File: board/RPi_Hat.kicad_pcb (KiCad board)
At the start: 2 copper layers, 65 x 56.5 mm, 5 parts, among them J1 RPi_GPIO

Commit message: first draft of the HAT layout
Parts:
- added C1: 10µF, Capacitors_SMD:c_elec_4x4.5, F.Cu at (113.4, 56.0)
- added C2: 0.1µF, Capacitors_SMD:C_0805_HandSoldering, F.Cu at (108.9, 56.4)
- added C3: 1µF, Capacitors_SMD:C_1206_HandSoldering, F.Cu at (127.5, 78.5)
- added C4: 1µF, Capacitors_SMD:C_1206_HandSoldering, F.Cu at (127.5, 73.0)
- added C5: 0.1µF, Capacitors_SMD:C_0805_HandSoldering, F.Cu at (133.0, 68.0)
- added C6: 0.1µF, Capacitors_SMD:C_0805_HandSoldering, F.Cu at (104.5, 72.0)
- added C7: 22pF, Capacitors_SMD:C_0603_HandSoldering, F.Cu at (106.0, 57.0)
- added C8: 22pF, Capacitors_SMD:C_0603_HandSoldering, F.Cu at (85.7, 56.9)
- added D1: SMD_LED, LEDs:LED-1206, F.Cu at (116.0, 93.5)
- added I1: TC1108, TO_SOT_Packages_SMD:SOT-223, F.Cu at (117.0, 75.5)
- added IC1: ATMEGA328P-P, Housings_DIP:DIP-28_W7.62mm, F.Cu at (117.5, 61.0)
- added IC2: RFM69HW, mysensors-kicad:RFM69HW_SMD_Handsoldering, F.Cu at (86.5, 95.0)
- added JPR1: NC_JPR, Pin_Headers:Pin_Header_Straight_1x02, F.Cu at (116.0, 85.5)
- added P1: FTDI_CONN_01X06, Pin_Headers:Pin_Header_Straight_1x06, F.Cu at (138.0, 55.5)
- added P2: BATT_IN, Pin_Headers:Pin_Header_Angled_1x02, F.Cu at (135.0, 74.5)
- added P3: V_SRC_JPR, Pin_Headers:Pin_Header_Straight_1x03, F.Cu at (128.5, 67.5)
- added P4: UART_SRC_JPR, Pin_Headers:Pin_Header_Straight_2x03, F.Cu at (125.0, 67.5)
- added P5: LED_CONN, Pin_Headers:Pin_Header_Straight_1x02, F.Cu at (116.0, 99.0)
- added P6: SW_CONN, Pin_Headers:Pin_Header_Straight_1x02, F.Cu at (130.5, 99.0)
- added P7: CONN_01X01, Pin_Headers:Pin_Header_Straight_1x01, F.Cu at (98.5, 74.0)
- added Q1: BSS138_GSD, TO_SOT_Packages_SMD:SOT-23_Handsoldering, F.Cu at (129.1, 55.7)
- added R1: 10K, Resistors_SMD:R_0805_HandSoldering, F.Cu at (124.9, 55.5)
- added R2: 10K, Resistors_SMD:R_0805_HandSoldering, F.Cu at (134.0, 55.6)
- added R3: 560R, Resistors_SMD:R_0603_HandSoldering, F.Cu at (116.0, 90.0)
- added R4: 10K, Resistors_SMD:R_0805_HandSoldering, F.Cu at (138.5, 87.5)
- added R5: 10K, Resistors_SMD:R_0805_HandSoldering, F.Cu at (133.0, 62.5)
- added SW1: SWITCH, Buttons_Switches_ThroughHole:SW_PUSH, F.Cu at (129.5, 88.0)
- added Y1: 16MHz, Crystals_Oscillators_SMD:Q_49U3HMS, F.Cu at (96.0, 56.0)
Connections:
- J1 pad 1: Net-(J1-Pad1) -> V3.3_PI
- J1 pad 10: Net-(J1-Pad10) -> RX_PI
- J1 pad 14: Net-(J1-Pad14) -> GND
- J1 pad 17: Net-(J1-Pad17) -> V3.3_PI
- J1 pad 20: Net-(J1-Pad20) -> GND
- J1 pad 25: Net-(J1-Pad25) -> GND
- J1 pad 30: Net-(J1-Pad30) -> GND
- J1 pad 34: Net-(J1-Pad34) -> GND
- J1 pad 39: Net-(J1-Pad39) -> GND
- J1 pad 6: Net-(J1-Pad6) -> GND
- J1 pad 8: Net-(J1-Pad8) -> TX_PI
- J1 pad 9: Net-(J1-Pad9) -> GND
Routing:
- net V3.3: track 0.00 -> 150.9 mm, vias 0 -> 2
- net SW_D3: track 0.00 -> 68.2 mm
- net LED_D9: track 0.00 -> 63.3 mm
- net V3.3_PI: track 0.00 -> 54.3 mm, vias 0 -> 2
- net D2_INT0: track 0.00 -> 50.4 mm, vias 0 -> 1
- net RX_PI: track 0.00 -> 47.1 mm, vias 0 -> 2
- net TX_PI: track 0.00 -> 46.4 mm, vias 0 -> 2
- net +BATT: track 0.00 -> 45.7 mm, vias 0 -> 1
- net TX_FTDI: track 0.00 -> 29.4 mm, vias 0 -> 2
- net Net-(C5-Pad2): track 0.00 -> 24.8 mm, vias 0 -> 1
- net RX_FTDI: track 0.00 -> 17.0 mm
- net TX_IN: track 0.00 -> 16.6 mm
- net TX_ARD: track 0.00 -> 15.2 mm
- net Net-(C8-Pad2): track 0.00 -> 13.0 mm
- net Net-(C7-Pad2): track 0.00 -> 12.8 mm
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
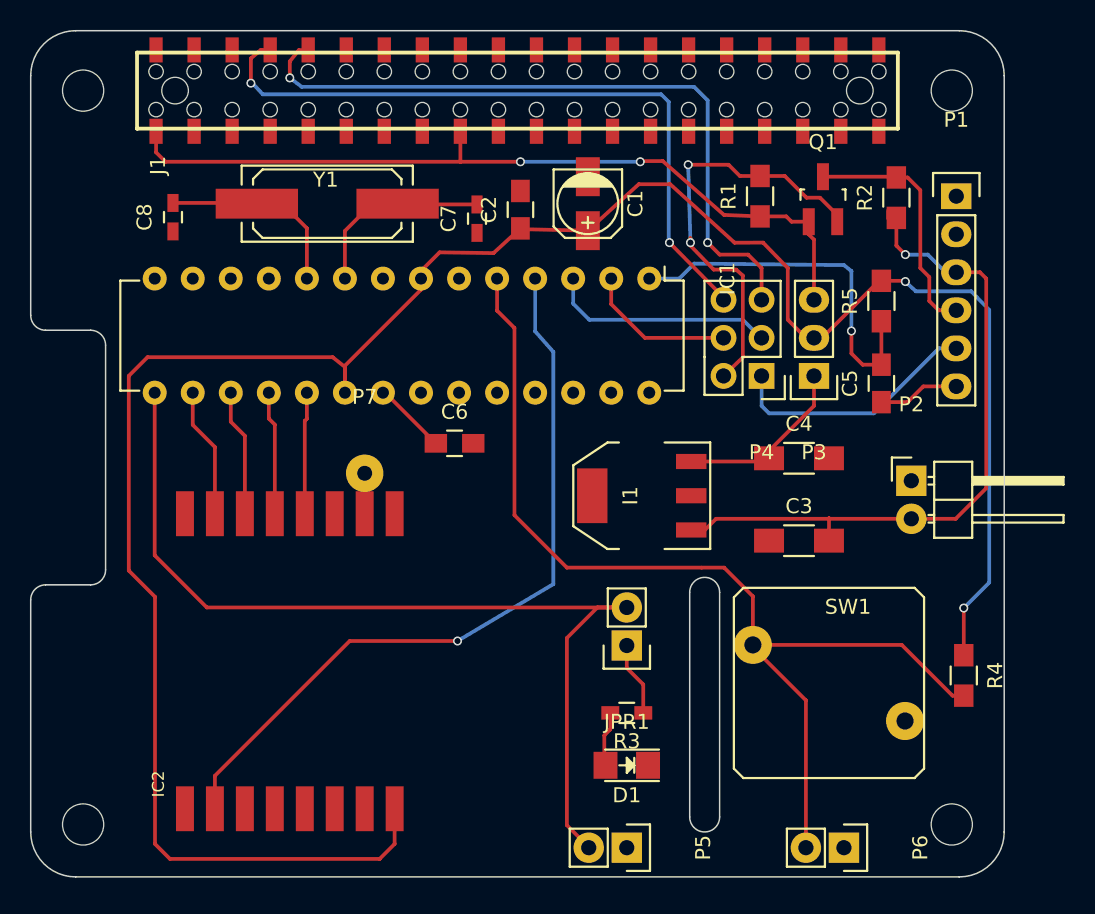
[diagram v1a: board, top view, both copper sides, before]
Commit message: board layout. check before manufacture
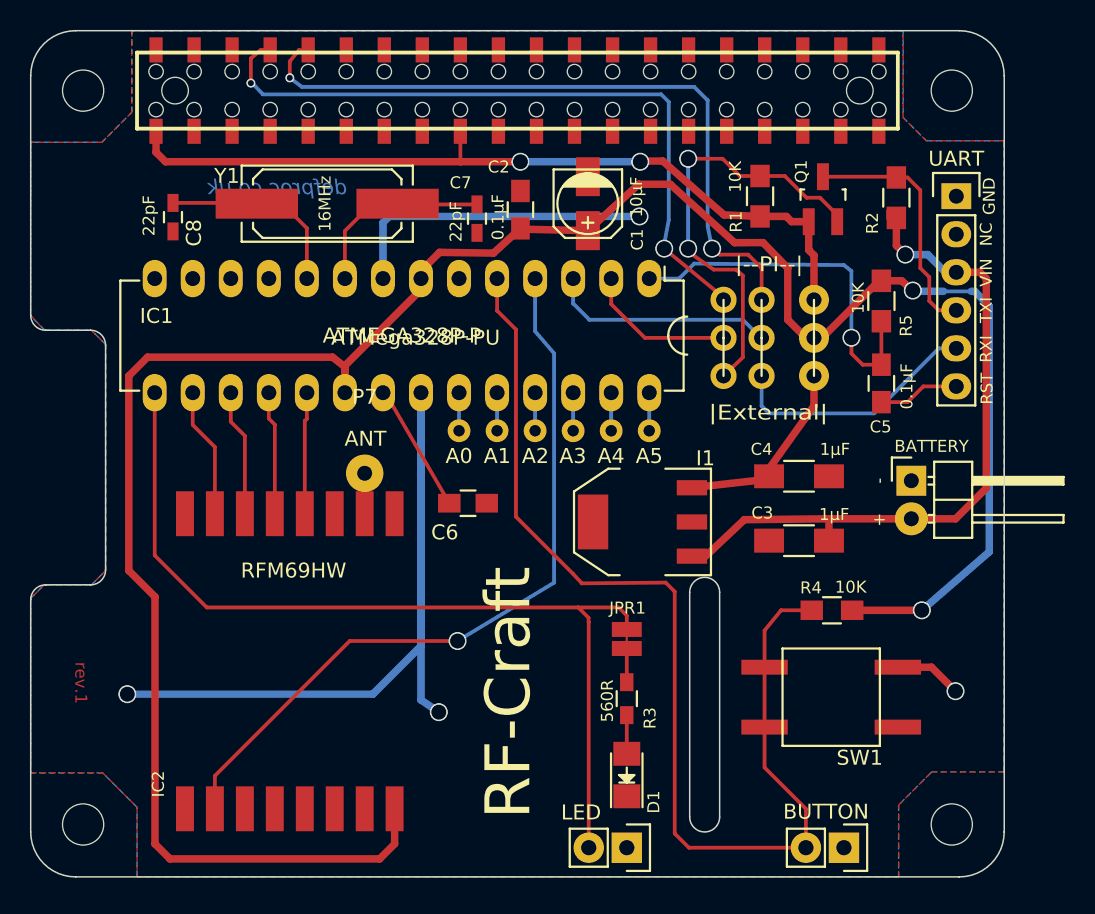
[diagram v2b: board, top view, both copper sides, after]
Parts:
- BATTERY: renamed from P2; footprint Pin_Headers:Pin_Header_Angled_1x02 -> Pin_Header_Angled_1x02
- BUTTON: renamed from P3; footprint Pin_Headers:Pin_Header_Straight_1x03 -> Pin_Header_Straight_1x03
- IC1: footprint Housings_DIP:DIP-28_W7.62mm -> A0-A5_DIP-28_W7.62mm
- JPR1: footprint Pin_Headers:Pin_Header_Straight_1x02 -> NC_SMD_JPR
- P: renamed from P4; footprint Pin_Headers:Pin_Header_Straight_2x03 -> Pin_Header_Straight_2x03
- SW1: footprint Buttons_Switches_ThroughHole:SW_PUSH -> KSEx00G_SW
- UART: renamed from P1; footprint Pin_Headers:Pin_Header_Straight_1x06 -> Pin_Header_Straight_1x06
- moved R4 9.82 mm to (129.7, 83.2), turned to 180 degrees
- moved C6 4.10 mm to (105.4, 76.0)
- moved I1 1.75 mm to (117.0, 77.2)
- moved C4 1.20 mm to (127.5, 74.2)
- moved SW1 0.96 mm to (129.7, 89.0)
- moved R3 0.95 mm to (116.0, 89.0), turned to 270 degrees
- moved D1 0.65 mm to (116.0, 94.2), turned to 90 degrees
- moved JPR1 0.20 mm to (116.0, 85.7)
- renumbered P5 to LED
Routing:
- net GND: track 0.00 -> 85.4 mm, vias 0 -> 4
- net SW_D3: track 68.2 -> 73.9 mm
- net Net-(C6-Pad1): track 4.93 -> 8.68 mm
- net V3.3: track 150.9 -> 154.0 mm
- net Net-(JPR1-Pad1): track 4.96 -> 2.25 mm
- net Net-(IC1-Pad28): track 0.00 -> 2.54 mm
- net Net-(IC1-Pad27): track 0.00 -> 2.54 mm
- net Net-(IC1-Pad26): track 0.00 -> 2.54 mm
- net Net-(IC1-Pad25): track 0.00 -> 2.54 mm
- net Net-(IC1-Pad24): track 0.00 -> 2.54 mm
- net Net-(IC1-Pad23): track 0.00 -> 2.54 mm
- net LED_D9: track 63.3 -> 61.3 mm
- net Net-(D1-Pad2): track 3.70 -> 2.58 mm
- net V3.3_BAT: track 12.0 -> 12.9 mm
- net TX_FTDI: track 29.4 -> 30.2 mm
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- added copper zone on B.Cu, net GND
- added copper zone on F.Cu, net GND
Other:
- net class BUS added: clearance 0.2, trace_width 0.5, via_dia 1.2, via_drill 1
- net class Default: via_dia 0.6 -> 1.2; via_drill 0.4 -> 1
- board text added: "+"
- board text added: "-"
- board text added: "0.1µF"
- board text added: "10K"
- board text added: "10µF"
- board text added: "16MHz"
- board text added: "1µF"
- board text added: "22pF"
- board text added: "560R"
- board text added: "ANT"
- board text added: "ATMega328P-PU"
- board text added: "Born in Liverpool"
- board text added: "GND"
- board text added: "NC"
- board text added: "RF-Craft"
- board text added: "RFM69HW"
- board text added: "RST"
- board text added: "RXI"
- board text added: "TXI"
- board text added: "VIN"
- board text added: "cheapjack.org.uk"
- board text added: "defproc.co.uk"
- board text added: "rev.1"
- board text added: "rev.1 2015-10-05"
- board text added: "|--PI--|"
- board text added: "|External|"

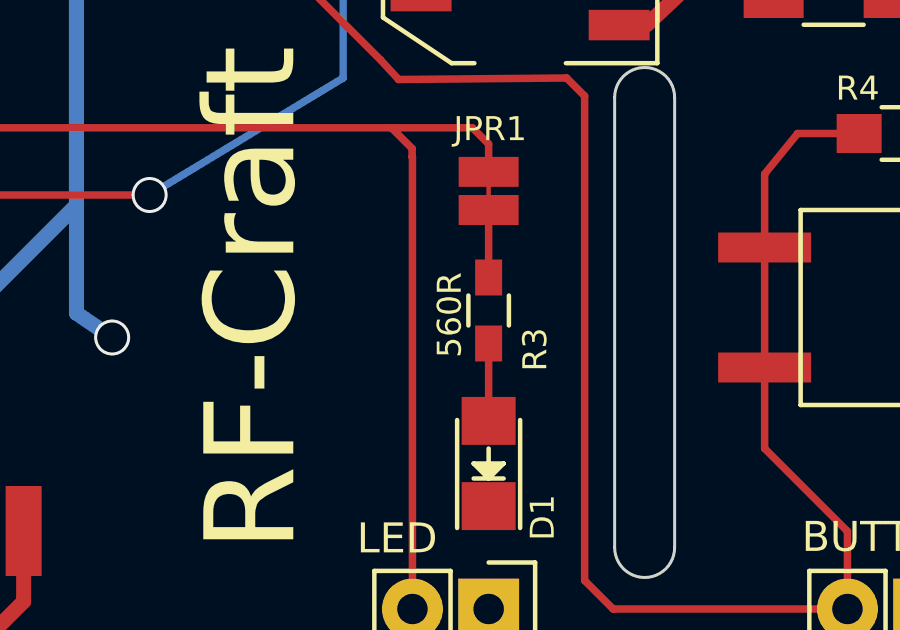
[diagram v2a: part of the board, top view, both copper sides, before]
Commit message: changed LED resistor to 75ohms (0603 package)
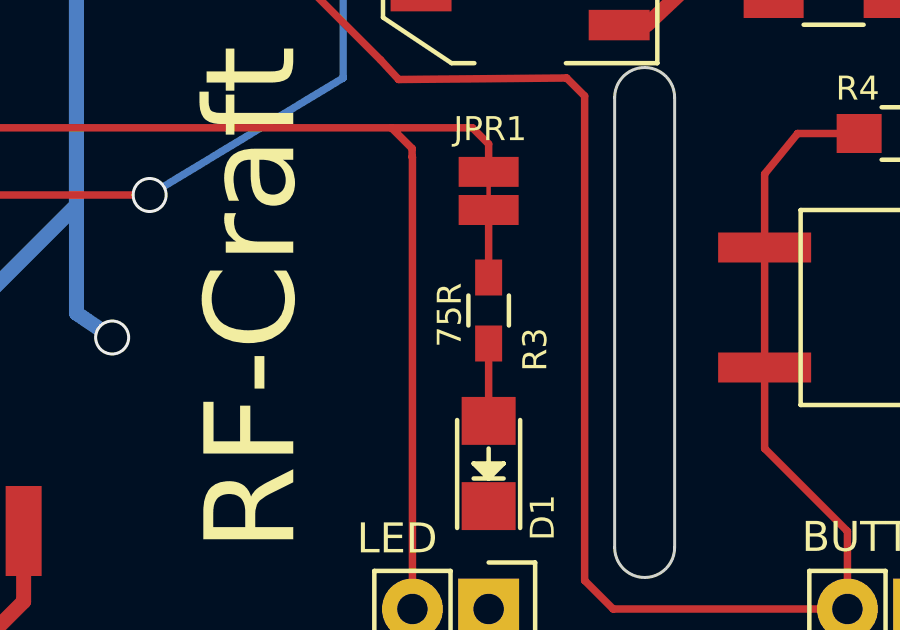
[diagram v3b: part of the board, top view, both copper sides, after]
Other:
- board text added: "75R"
- board text removed: "560R"
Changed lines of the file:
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@@
     (effects (font (size 1 1) (thickness 0.15)))
   )
-  (gr_text 560R (at 114.7 89.2 90) (layer F.SilkS)
+  (gr_text 75R (at 114.7 89.2 90) (layer F.SilkS)
     (effects (font (size 0.8 0.8) (thickness 0.15)))
   )
